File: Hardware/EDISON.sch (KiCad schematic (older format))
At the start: 5 parts, among them P5 CONN_01X06, SW2 PWR_BTN, U18 EdisonConnector

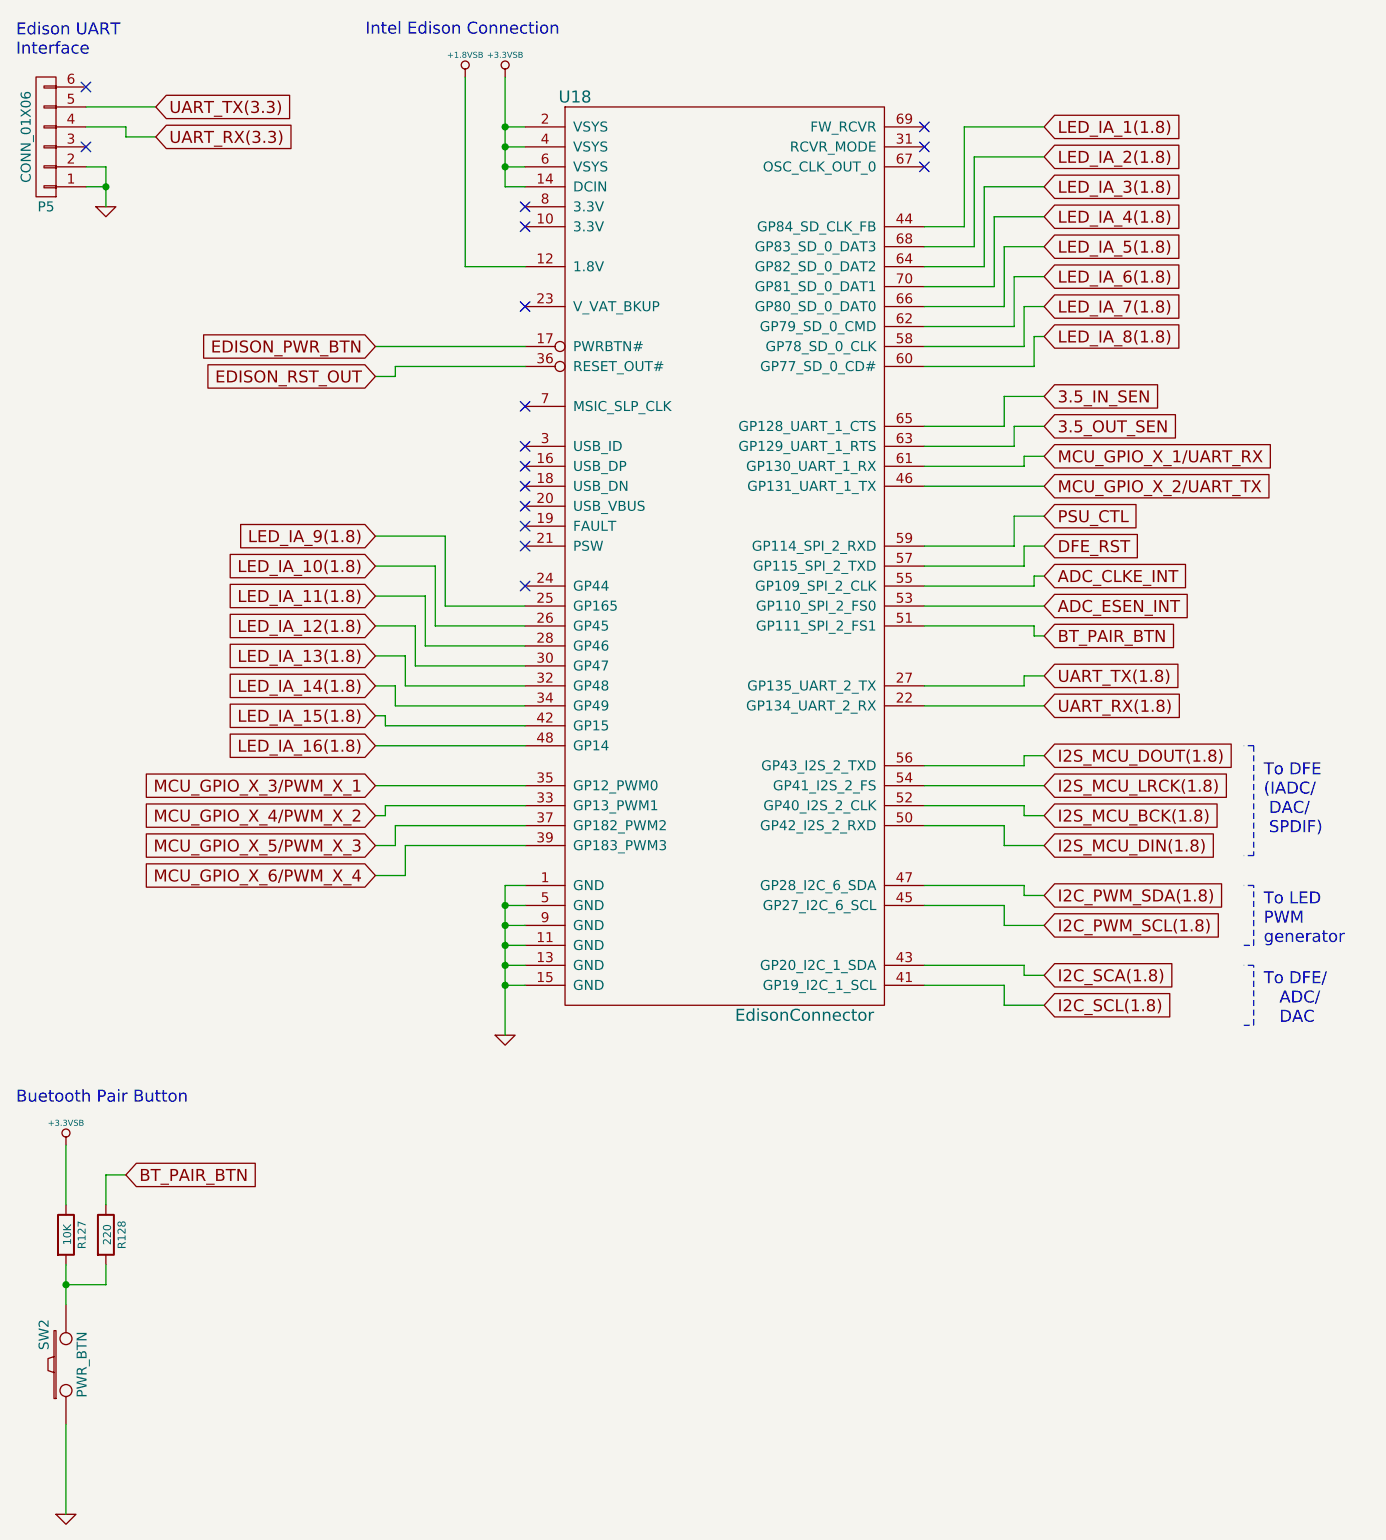
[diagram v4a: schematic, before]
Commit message: Completed placement of level shifters
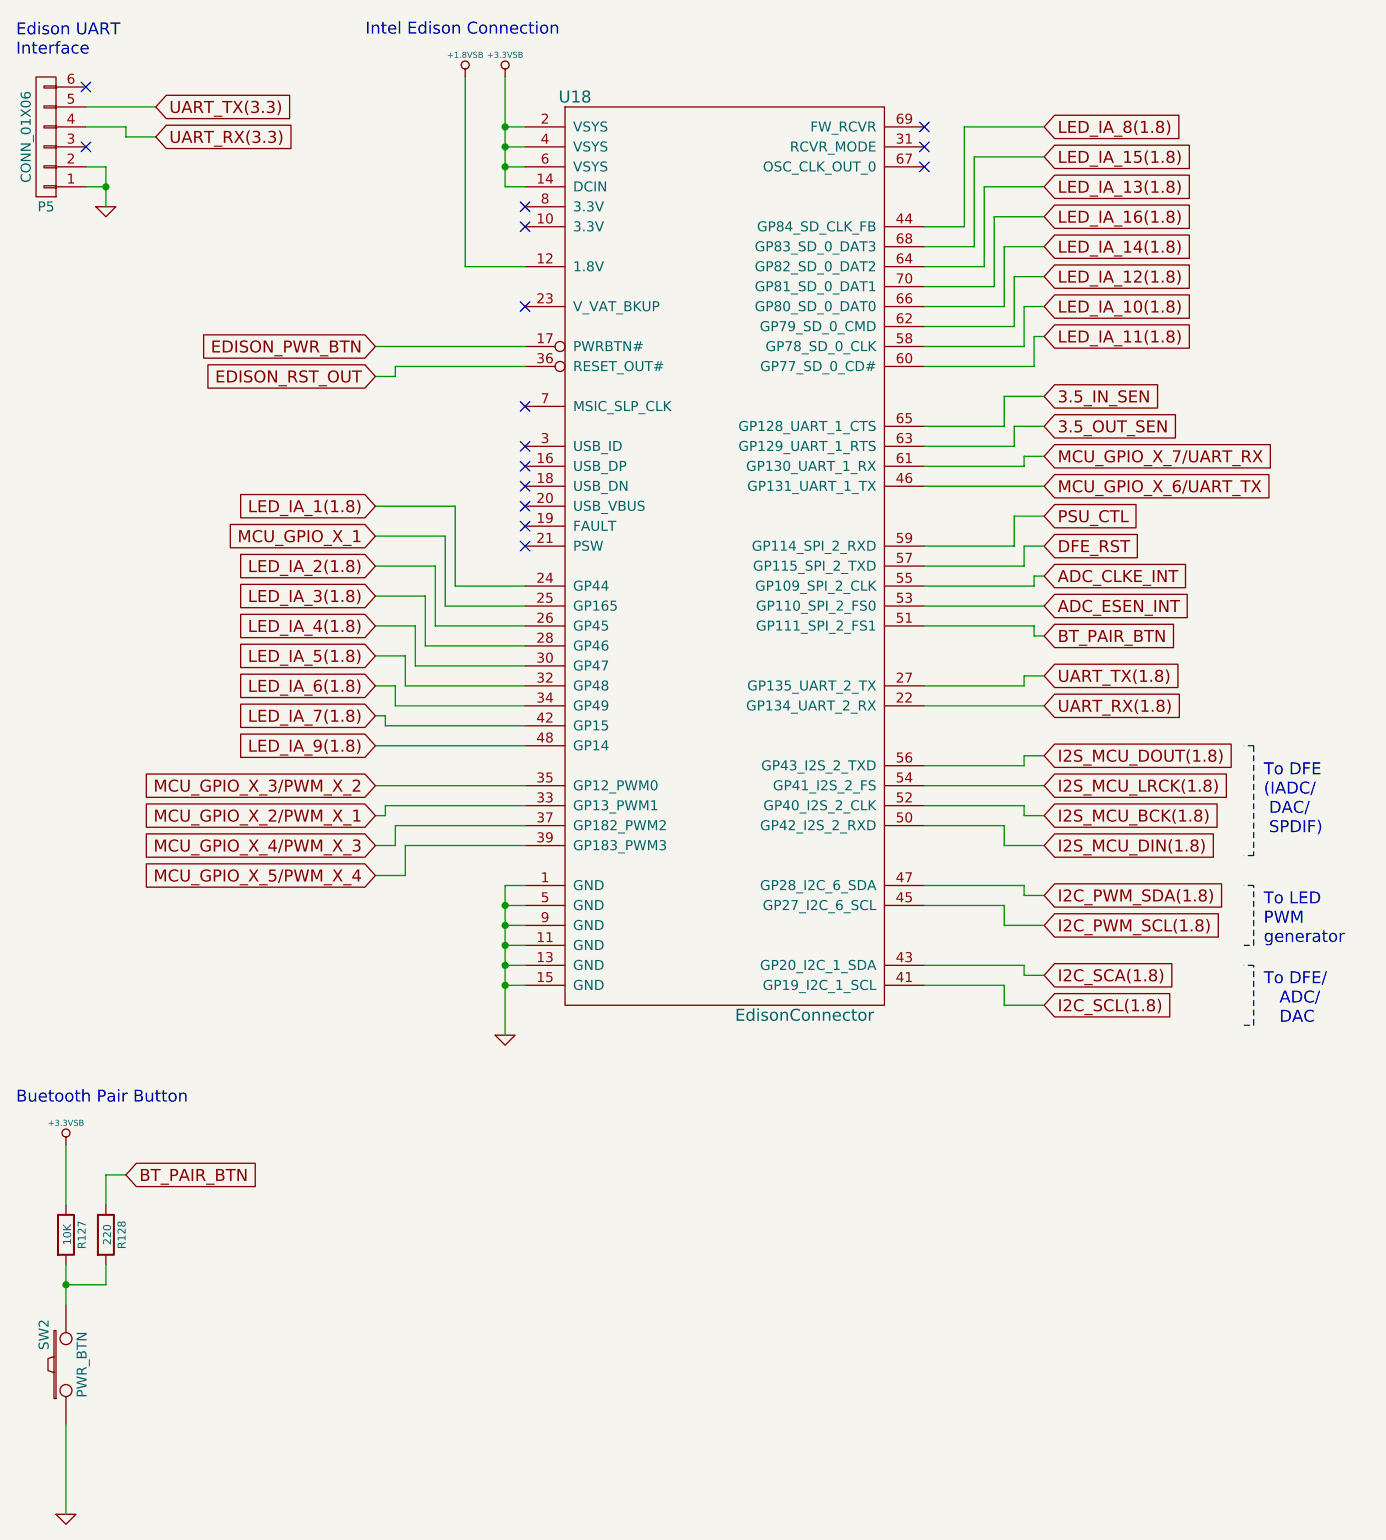
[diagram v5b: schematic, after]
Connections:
- net LED_IA_1(1.8): now also U18.24 (GP44); no longer U18.44 (GP84_SD_CLK_FB)
- net LED_IA_10(1.8): now also U18.58 (GP78_SD_0_CLK); no longer U18.26 (GP45)
- net LED_IA_11(1.8): now also U18.60 (GP77_SD_0_CD#); no longer U18.28 (GP46)
- net LED_IA_12(1.8): now also U18.62 (GP79_SD_0_CMD); no longer U18.30 (GP47)
- net LED_IA_13(1.8): now also U18.64 (GP82_SD_0_DAT2); no longer U18.32 (GP48)
- net LED_IA_14(1.8): now also U18.66 (GP80_SD_0_DAT0); no longer U18.34 (GP49)
- net LED_IA_15(1.8): now also U18.68 (GP83_SD_0_DAT3); no longer U18.42 (GP15)
- net LED_IA_16(1.8): now also U18.70 (GP81_SD_0_DAT1); no longer U18.48 (GP14)
- net LED_IA_2(1.8): now also U18.26 (GP45); no longer U18.68 (GP83_SD_0_DAT3)
- net LED_IA_3(1.8): now also U18.28 (GP46); no longer U18.64 (GP82_SD_0_DAT2)
- net LED_IA_4(1.8): now also U18.30 (GP47); no longer U18.70 (GP81_SD_0_DAT1)
- net LED_IA_5(1.8): now also U18.32 (GP48); no longer U18.66 (GP80_SD_0_DAT0)
- net LED_IA_6(1.8): now also U18.34 (GP49); no longer U18.62 (GP79_SD_0_CMD)
- net LED_IA_7(1.8): now also U18.42 (GP15); no longer U18.58 (GP78_SD_0_CLK)
- net LED_IA_8(1.8): now also U18.44 (GP84_SD_CLK_FB); no longer U18.60 (GP77_SD_0_CD#)
- net LED_IA_9(1.8): now also U18.48 (GP14); no longer U18.25 (GP165)
- net MCU_GPIO_X_1/UART_RX renamed MCU_GPIO_X_7/UART_RX
- net MCU_GPIO_X_2/UART_TX renamed MCU_GPIO_X_6/UART_TX
- net MCU_GPIO_X_3/PWM_X_1 renamed MCU_GPIO_X_3/PWM_X_2
- net MCU_GPIO_X_4/PWM_X_2 renamed MCU_GPIO_X_2/PWM_X_1
- net MCU_GPIO_X_5/PWM_X_3 renamed MCU_GPIO_X_4/PWM_X_3
- net MCU_GPIO_X_6/PWM_X_4 renamed MCU_GPIO_X_5/PWM_X_4
- new net MCU_GPIO_X_1: U18.25 (GP165)
- no-connect marks 16 -> 15
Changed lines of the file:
@@
 Comment4 ""
 $EndDescr
-$Comp
-L EdisonConnector U18
-U 1 1 57F8CAB1
-P 3650 1550
-F 0 "U18" H 3700 1600 60  0000 C CNN
-F 1 "EdisonConnector" H 4850 -3000 60  0000 C CNN
-F 2 "muse-v2-lib:Intel_Edison" H 3650 1950 60  0001 C CNN
-F 3 "" H 3650 1950 60  0000 C CNN
-	1    3650 1550
-	1    0    0    -1
-$EndComp
 Text Notes 7150 5200 0    60   ~ 0
 To DFE\n(IADC/\n DAC/\n SPDIF)
@@
 Wire Wire Line
 	2800 2850 3450 2850
-Text GLabel 2700 3700 0    60   Input ~ 0
+Text GLabel 2700 4750 0    60   Input ~ 0
 LED_IA_9(1.8)
+Text GLabel 6050 2550 2    60   Input ~ 0
+LED_IA_10(1.8)
+Text GLabel 6050 2700 2    60   Input ~ 0
+LED_IA_11(1.8)
+Text GLabel 6050 2400 2    60   Input ~ 0
+LED_IA_12(1.8)
+Text GLabel 6050 1950 2    60   Input ~ 0
+LED_IA_13(1.8)
+Text GLabel 6050 2250 2    60   Input ~ 0
+LED_IA_14(1.8)
+Text GLabel 6050 1800 2    60   Input ~ 0
+LED_IA_15(1.8)
+Text GLabel 6050 2100 2    60   Input ~ 0
+LED_IA_16(1.8)
+Text GLabel 2700 3550 0    60   Input ~ 0
+LED_IA_1(1.8)
 Text GLabel 2700 3850 0    60   Input ~ 0
-LED_IA_10(1.8)
+LED_IA_2(1.8)
 Text GLabel 2700 4000 0    60   Input ~ 0
-LED_IA_11(1.8)
+LED_IA_3(1.8)
 Text GLabel 2700 4150 0    60   Input ~ 0
-LED_IA_12(1.8)
+LED_IA_4(1.8)
 Text GLabel 2700 4300 0    60   Input ~ 0
-LED_IA_13(1.8)
+LED_IA_5(1.8)
 Text GLabel 2700 4450 0    60   Input ~ 0
-LED_IA_14(1.8)
+LED_IA_6(1.8)
 Text GLabel 2700 4600 0    60   Input ~ 0
-LED_IA_15(1.8)
-Text GLabel 2700 4750 0    60   Input ~ 0
-LED_IA_16(1.8)
+LED_IA_7(1.8)
 Text GLabel 6050 1650 2    60   Input ~ 0
-LED_IA_1(1.8)
-Text GLabel 6050 1800 2    60   Input ~ 0
-LED_IA_2(1.8)
-Text GLabel 6050 1950 2    60   Input ~ 0
-LED_IA_3(1.8)
-Text GLabel 6050 2100 2    60   Input ~ 0
-LED_IA_4(1.8)
-Text GLabel 6050 2250 2    60   Input ~ 0
-LED_IA_5(1.8)
-Text GLabel 6050 2400 2    60   Input ~ 0
-LED_IA_6(1.8)
-Text GLabel 6050 2550 2    60   Input ~ 0
-LED_IA_7(1.8)
-Text GLabel 6050 2700 2    60   Input ~ 0
 LED_IA_8(1.8)
 Text GLabel 6050 4400 2    60   Input ~ 0
@@
 	5850 5950 5450 5950
 Text GLabel 6050 3300 2    60   Input ~ 0
-MCU_GPIO_X_1/UART_RX
+MCU_GPIO_X_7/UART_RX
 Text GLabel 6050 3450 2    60   Input ~ 0
-MCU_GPIO_X_2/UART_TX
+MCU_GPIO_X_6/UART_TX
 Text GLabel 6050 3600 2    60   Input ~ 0
 PSU_CTL
@@
 Wire Wire Line
 	3050 3700 2700 3700
+Text GLabel 2700 5100 0    60   Input ~ 0
+MCU_GPIO_X_2/PWM_X_1
+Wire Wire Line
+	2700 4950 3450 4950
 Text GLabel 2700 4950 0    60   Input ~ 0
-MCU_GPIO_X_3/PWM_X_1
-Wire Wire Line
-	2700 4950 3450 4950
-Text GLabel 2700 5100 0    60   Input ~ 0
-MCU_GPIO_X_4/PWM_X_2
+MCU_GPIO_X_3/PWM_X_2
 Text GLabel 2700 5250 0    60   Input ~ 0
-MCU_GPIO_X_5/PWM_X_3
+MCU_GPIO_X_4/PWM_X_3
 Text GLabel 2700 5400 0    60   Input ~ 0
-MCU_GPIO_X_6/PWM_X_4
+MCU_GPIO_X_5/PWM_X_4
 Wire Wire Line
 	2700 5100 2750 5100
@@
 Text Notes 900  6550 0    60   ~ 0
 Buetooth Pair Button
-NoConn ~ 3450 3950
 Text GLabel 6050 3000 2    60   Input ~ 0
 3.5_IN_SEN
 Text GLabel 6050 3150 2    60   Input ~ 0
 3.5_OUT_SEN
+$Comp
+L EdisonConnector U18
+U 1 1 57F8CAB1
+P 3650 1550
+F 0 "U18" H 3700 1600 60  0000 C CNN
+F 1 "EdisonConnector" H 4850 -3000 60  0000 C CNN
+F 2 "muse-v2-lib:Intel_Edison" H 3650 1950 60  0001 C CNN
+F 3 "" H 3650 1950 60  0000 C CNN
+	1    3650 1550
+	1    0    0    -1
+$EndComp
+Text GLabel 2700 3700 0    60   Input ~ 0
+MCU_GPIO_X_1
+Wire Wire Line
+	2700 3550 3100 3550
+Wire Wire Line
+	3100 3550 3100 3950
+Wire Wire Line
+	3100 3950 3450 3950
 $EndSCHEMATC

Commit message: Digital Half completed placement
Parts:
- SW2: value PWR_BTN -> PAIR_BTN
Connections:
- net MCU_GPIO_X_1: no longer names the net of U18.25 (GP165)
- no-connect marks 15 -> 16

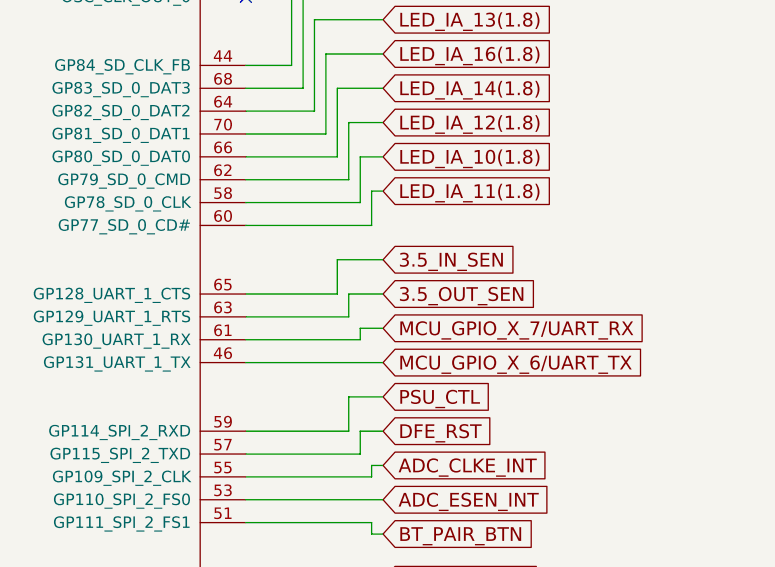
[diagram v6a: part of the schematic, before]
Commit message: Mounting holes added
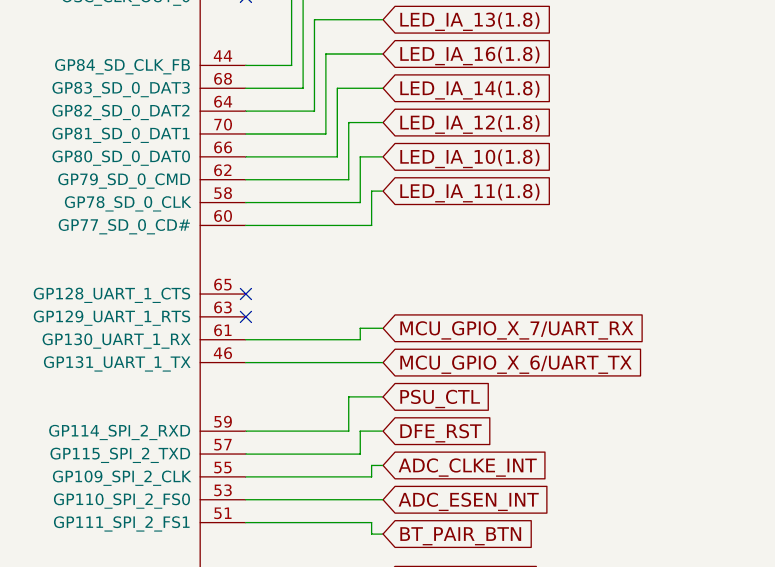
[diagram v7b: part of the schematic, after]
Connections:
- net 3.5_IN_SEN: no longer names the net of U18.65 (GP128_UART_1_CTS)
- net 3.5_OUT_SEN: no longer names the net of U18.63 (GP129_UART_1_RTS)
- no-connect marks 16 -> 18
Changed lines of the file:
@@
 Text Notes 900  6550 0    60   ~ 0
 Buetooth Pair Button
-Text GLabel 6050 3000 2    60   Input ~ 0
-3.5_IN_SEN
-Text GLabel 6050 3150 2    60   Input ~ 0
-3.5_OUT_SEN
 $Comp
 L EdisonConnector U18
@@
 	5950 3300 6050 3300
 Wire Wire Line
-	5450 3250 5900 3250
-Wire Wire Line
-	5900 3250 5900 3150
-Wire Wire Line
-	5900 3150 6050 3150
-Wire Wire Line
-	5450 3150 5850 3150
-Wire Wire Line
-	5850 3150 5850 3000
-Wire Wire Line
-	5850 3000 6050 3000
-Wire Wire Line
 	5450 2850 6000 2850
 Wire Wire Line
@@
 Wire Wire Line
 	3100 3950 3450 3950
+NoConn ~ 5450 3250
+NoConn ~ 5450 3150
 $EndSCHEMATC
